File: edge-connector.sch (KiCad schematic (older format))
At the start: 1 part

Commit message: Initial component placement added (to be adjusted further)
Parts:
- renumbered J to J9
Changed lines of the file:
@@
 $EndDescr
 $Comp
-L antmicroPciConnectors:SFF-TA-1002-4C+ J
+L antmicroPciConnectors:SFF-TA-1002-4C+ J9
 U 1 1 625AED2C
 P 7875 1425
-F 0 "J" H 7875 1590 50  0000 C CNN
+F 0 "J9" H 7875 1590 50  0000 C CNN
 F 1 "SFF-TA-1002-4C+" H 7875 1499 50  0000 C CNN
 F 2 "antmicro-footprints:SFF-TA-1002-4C+" H 8275 1475 50  0001 C CNN
@@
 Connection ~ 6925 10425
 $Comp
-L power:GND #PWR?
+L power:GND #PWR082
 U 1 1 626F241B
 P 6925 10625
-F 0 "#PWR?" H 6925 10375 50  0001 C CNN
+F 0 "#PWR082" H 6925 10375 50  0001 C CNN
 F 1 "GND" H 6930 10452 50  0000 C CNN
 F 2 "" H 6925 10625 50  0001 C CNN
@@
 	8825 10425 8825 10625
 $Comp
-L power:GND #PWR?
+L power:GND #PWR083
 U 1 1 62BB82B7
 P 8825 10625
-F 0 "#PWR?" H 8825 10375 50  0001 C CNN
+F 0 "#PWR083" H 8825 10375 50  0001 C CNN
 F 1 "GND" H 8830 10452 50  0000 C CNN
 F 2 "" H 8825 10625 50  0001 C CNN

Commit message: Update after designator unification
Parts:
- renumbered J9 to J5
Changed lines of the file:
@@
 $Descr A3 16535 11693
 encoding utf-8
-Sheet 8 10
+Sheet 5 10
 Title ""
 Date ""
@@
 $EndDescr
 $Comp
-L antmicroPciConnectors:SFF-TA-1002-4C+ J9
+L antmicroPciConnectors:SFF-TA-1002-4C+ J5
 U 1 1 625AED2C
 P 7875 1425
-F 0 "J9" H 7875 1590 50  0000 C CNN
+F 0 "J5" H 7875 1590 50  0000 C CNN
 F 1 "SFF-TA-1002-4C+" H 7875 1499 50  0000 C CNN
 F 2 "antmicro-footprints:SFF-TA-1002-4C+" H 8275 1475 50  0001 C CNN
@@
 Connection ~ 6925 10425
 $Comp
-L power:GND #PWR082
+L power:GND #PWR026
 U 1 1 626F241B
 P 6925 10625
-F 0 "#PWR082" H 6925 10375 50  0001 C CNN
+F 0 "#PWR026" H 6925 10375 50  0001 C CNN
 F 1 "GND" H 6930 10452 50  0000 C CNN
 F 2 "" H 6925 10625 50  0001 C CNN
@@
 	8825 10425 8825 10625
 $Comp
-L power:GND #PWR083
+L power:GND #PWR027
 U 1 1 62BB82B7
 P 8825 10625
-F 0 "#PWR083" H 8825 10375 50  0001 C CNN
+F 0 "#PWR027" H 8825 10375 50  0001 C CNN
 F 1 "GND" H 8830 10452 50  0000 C CNN
 F 2 "" H 8825 10625 50  0001 C CNN

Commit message: Add local component libraries
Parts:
- J5: footprint antmicro-footprints:SFF-TA-1002-4C+ -> artix-dc-scm-footprints:SFF-TA-1002-4C+; symbol antmicroPciConnectors:SFF-TA-1002-4C+ -> artix-dc-scm:SFF-TA-1002-4C+
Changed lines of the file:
@@
 $Descr A3 16535 11693
 encoding utf-8
-Sheet 5 10
+Sheet 7 10
 Title ""
 Date ""
@@
 $EndDescr
 $Comp
-L antmicroPciConnectors:SFF-TA-1002-4C+ J5
+L artix-dc-scm:SFF-TA-1002-4C+ J5
 U 1 1 625AED2C
 P 7875 1425
 F 0 "J5" H 7875 1590 50  0000 C CNN
 F 1 "SFF-TA-1002-4C+" H 7875 1499 50  0000 C CNN
-F 2 "antmicro-footprints:SFF-TA-1002-4C+" H 8275 1475 50  0001 C CNN
+F 2 "artix-dc-scm-footprints:SFF-TA-1002-4C+" H 8275 1475 50  0001 C CNN
 F 3 "https://cdn.amphenol-icc.com/media/wysiwyg/files/documentation/sme005.pdf?__cf_chl_jschl_tk__=4604d1306574a1ee474ea914090d3e0c57e266a6-1606907014-0-AbkYBTCTl__kMBcY3BDmgKpfUy32FqitwN2Lniuy8W-uyv2Ev04Q-Q5Mr7srIz_Wnur0_9chB4CRbxKSYcEh7IvAJYsUgJ0PWIS5YdRqqHg567uaZciEX2hQP4ss5l6M4XdNrxEjJppHvyRV3ku89t-VmUSzhgCb8oJlyHpTxST4dEmKZNXfM53TM0tmGirdVbCRt1Byrx5pkz_uMvNABIOj7B2-eDGK52J3DWRD76zEyjdxY7Iz11gPiOY5i_QGIR3uOwkR5LBPNXe8zGqAf8--AKa7RqDbIriQRt90_32C4zIuHqbGa05BXS135E65ov80PbVcb4eSiutCqcJUAacUwu3eVnXVeIumfihJxuP8Rv7_n6saeG_2IuQpEiskzovLGKZM3667Y-rm-AL1NRXTamtvBxqTk0vyMvZ60FgJ" H 7875 1525 50  0001 C CNN
 	1    7875 1425
@@
 Connection ~ 6925 10425
 $Comp
-L power:GND #PWR026
+L artix-dc-scm:GND #PWR026
 U 1 1 626F241B
 P 6925 10625
@@
 	8825 10425 8825 10625
 $Comp
-L power:GND #PWR027
+L artix-dc-scm:GND #PWR027
 U 1 1 62BB82B7
 P 8825 10625

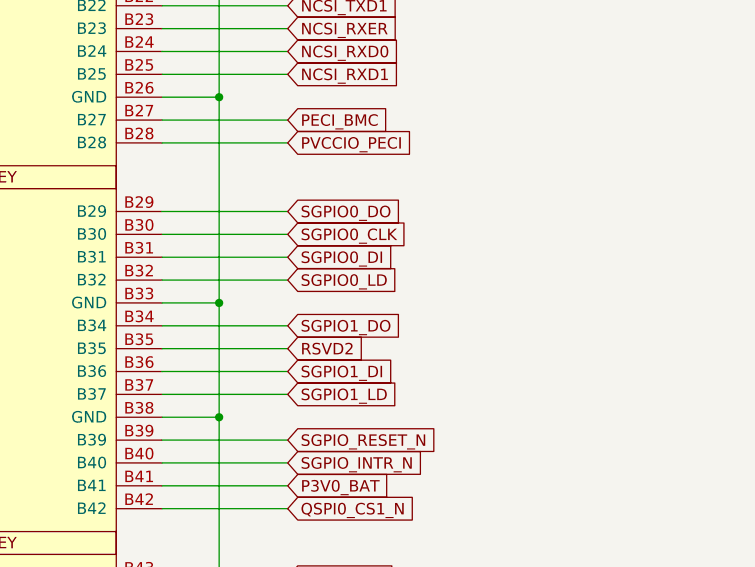
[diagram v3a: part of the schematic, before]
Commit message: Fixes after review (pin connections)
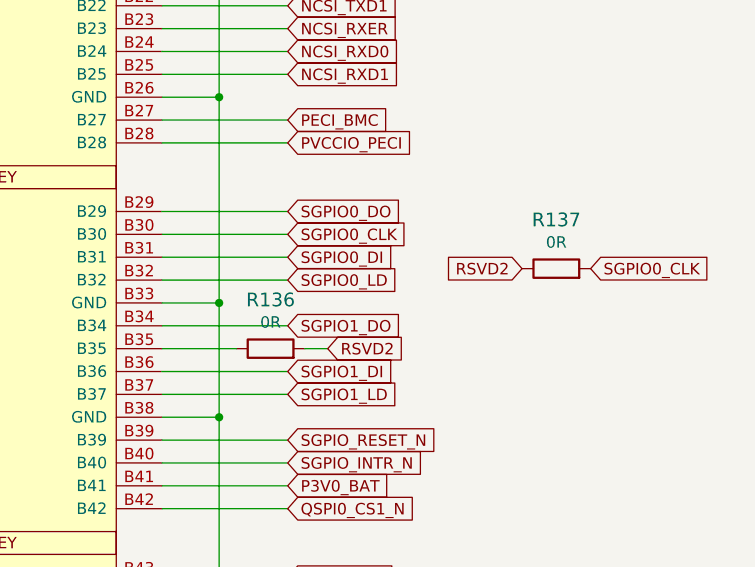
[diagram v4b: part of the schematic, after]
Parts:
- added R136, R137: R_0R_0402, antmicro-footprints:0402-res, symbol artix-dc-scm:R_0R_0402
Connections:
- net RSVD2: now also R136.2, R137.1; no longer J5.B35
- net SGPIO0_CLK: now also R137.2
- new net: J5.B35, R136.1
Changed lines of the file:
@@
 	9125 6125 8575 6125
 Wire Wire Line
-	9125 6225 8575 6225
-Wire Wire Line
 	8575 6325 9125 6325
 Wire Wire Line
@@
 Wire Wire Line
 	8575 6625 9125 6625
-Wire Wire Line
-	9125 6725 8575 6725
 Wire Wire Line
 	9125 6825 8575 6825
@@
 Text GLabel 9125 6625 2    50   Input ~ 0
 SGPIO1_DO
-Text GLabel 9125 6725 2    50   Input ~ 0
+Text GLabel 9300 6725 2    50   Input ~ 0
 RSVD2
 Text GLabel 9125 6825 2    50   Input ~ 0
@@
 	1    0    0    -1
 $EndComp
+$Comp
+L artix-dc-scm:R_0R_0402 R136
+U 1 1 616ABCDE
+P 9050 6725
+F 0 "R136" H 9050 6938 60  0000 C CNN
+F 1 "R_0R_0402" H 9050 6575 60  0001 C CNN
+F 2 "antmicro-footprints:0402-res" H 9250 6925 60  0001 L CNN
+F 3 "" H 9050 6725 50  0001 C CNN
+F 4 "PANASONIC" H 9250 7125 60  0001 L CNN "Manufacturer"
+F 5 "ERJ2GE0R00X" H 9250 7025 60  0001 L CNN "MPN"
+F 6 "0R" H 9050 6840 50  0000 C CNN "Val"
+	1    9050 6725
+	1    0    0    -1
+$EndComp
+Wire Wire Line
+	9300 6725 9200 6725
+Wire Wire Line
+	8575 6725 8900 6725
+Wire Wire Line
+	8575 6225 9125 6225
+Text GLabel 10150 6375 0    50   Input ~ 0
+RSVD2
+Text GLabel 10450 6375 2    50   Input ~ 0
+SGPIO0_CLK
+$Comp
+L artix-dc-scm:R_0R_0402 R137
+U 1 1 617019A6
+P 10300 6375
+F 0 "R137" H 10300 6588 60  0000 C CNN
+F 1 "R_0R_0402" H 10300 6225 60  0001 C CNN
+F 2 "antmicro-footprints:0402-res" H 10500 6575 60  0001 L CNN
+F 3 "" H 10300 6375 50  0001 C CNN
+F 4 "PANASONIC" H 10500 6775 60  0001 L CNN "Manufacturer"
+F 5 "ERJ2GE0R00X" H 10500 6675 60  0001 L CNN "MPN"
+F 6 "0R" H 10300 6490 50  0000 C CNN "Val"
+	1    10300 6375
+	1    0    0    -1
+$EndComp

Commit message: Update component libraries
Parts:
- R136, R137: footprint antmicro-footprints:0402-res -> artix-dc-scm-footprints:0402-res
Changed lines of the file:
@@
 Connection ~ 6925 10425
 $Comp
-L artix-dc-scm:GND #PWR026
+L artix-dc-scm:GND-artix-dc-scm #PWR026
 U 1 1 626F241B
 P 6925 10625
@@
 	8825 10425 8825 10625
 $Comp
-L artix-dc-scm:GND #PWR027
+L artix-dc-scm:GND-artix-dc-scm #PWR027
 U 1 1 62BB82B7
 P 8825 10625
@@
 F 0 "R136" H 9050 6938 60  0000 C CNN
 F 1 "R_0R_0402" H 9050 6575 60  0001 C CNN
-F 2 "antmicro-footprints:0402-res" H 9250 6925 60  0001 L CNN
+F 2 "artix-dc-scm-footprints:0402-res" H 9250 6925 60  0001 L CNN
 F 3 "" H 9050 6725 50  0001 C CNN
 F 4 "PANASONIC" H 9250 7125 60  0001 L CNN "Manufacturer"
@@
 F 0 "R137" H 10300 6588 60  0000 C CNN
 F 1 "R_0R_0402" H 10300 6225 60  0001 C CNN
-F 2 "antmicro-footprints:0402-res" H 10500 6575 60  0001 L CNN
+F 2 "artix-dc-scm-footprints:0402-res" H 10500 6575 60  0001 L CNN
 F 3 "" H 10300 6375 50  0001 C CNN
 F 4 "PANASONIC" H 10500 6775 60  0001 L CNN "Manufacturer"
